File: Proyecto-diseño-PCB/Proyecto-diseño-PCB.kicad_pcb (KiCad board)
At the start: 4 copper layers, 76 x 35 mm, 41 parts, among them J1 USB_B_Micro, J2 PROGRAMACIÓN/DEPURACIÓN, J3 LADO A, J4 LADO B, SW1 BOTON, SW2 BOTON, SW3 RESET, U1 TPD2EUSB30, U2 LP2950-3.3_TO252, U3 PIC18LF45K50-I/P

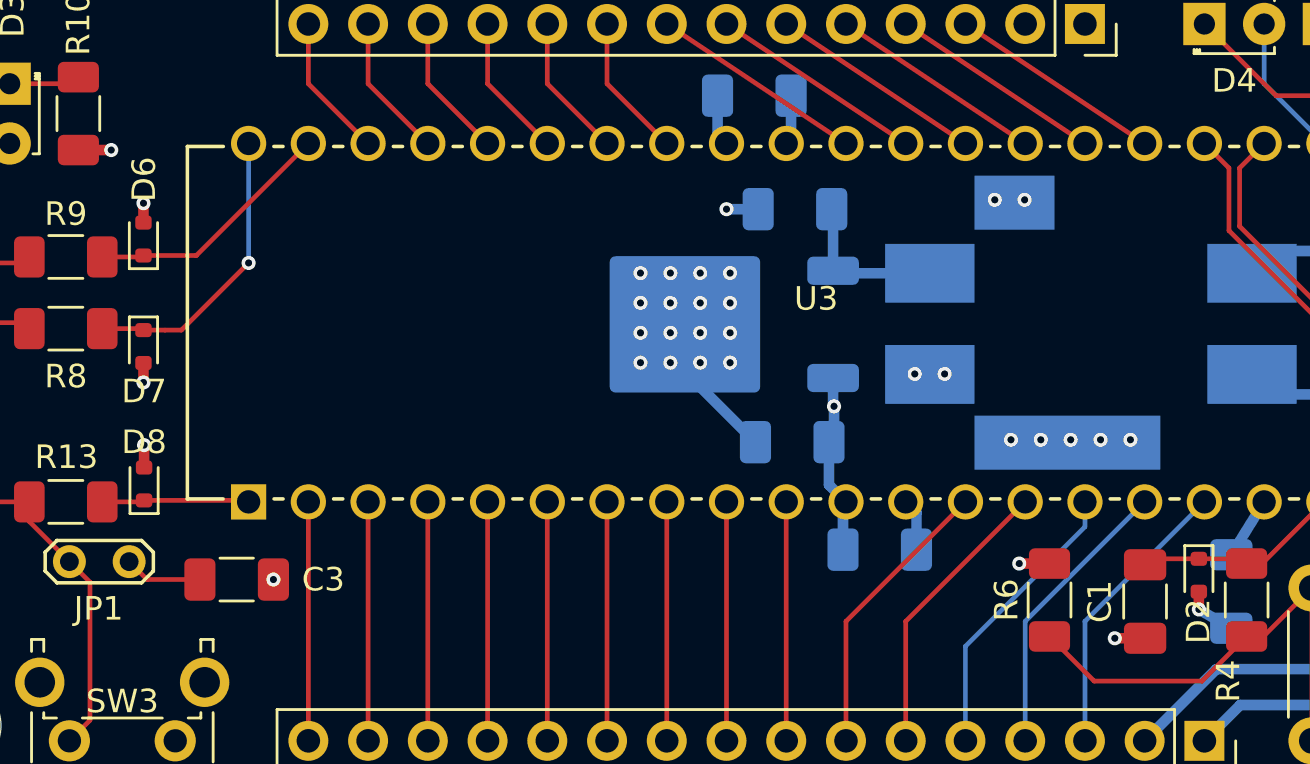
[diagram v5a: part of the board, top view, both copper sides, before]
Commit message: Correccion: agregue isla para disipacion de calor
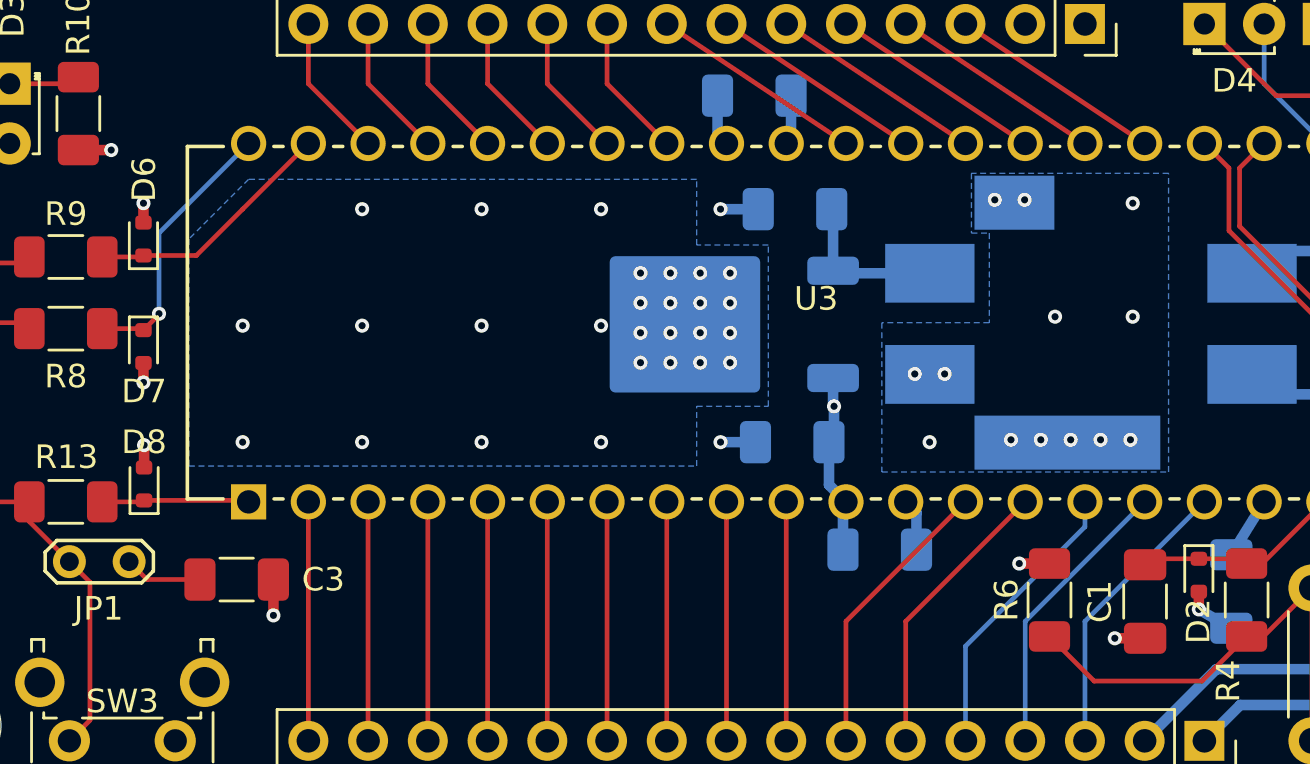
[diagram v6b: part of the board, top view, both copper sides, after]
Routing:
- net GND: track 41.0 -> 40.0 mm, vias 39 -> 55
- net /PGD: track 12.5 -> 11.6 mm
- added copper zone on B.Cu, net GND
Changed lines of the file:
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@@
 		(allow_soldermask_bridges_in_footprints no)
 		(tenting front back)
-		(grid_origin 164.719 98.298)
+		(grid_origin 124.079 88.138)
 		(pcbplotparams
 			(layerselection 0x00000000_00000000_55555555_55555555)
@@
 	)
 	(segment
+		(start 125.1335 92.964)
+		(end 125.1335 91.44)
+		(width 0.45)
+		(layer "F.Cu")
+		(net 1)
+	)
+	(segment
 		(start 176.911 87.692)
 		(end 176.911 86.868)
@@
 	)
 	(via
+		(at 128.905 85.598)
+		(size 0.6)
+		(drill 0.3)
+		(layers "F.Cu" "B.Cu")
+		(free yes)
+		(net 1)
+	)
+	(via
+		(at 161.671 75.438)
+		(size 0.6)
+		(drill 0.3)
+		(layers "F.Cu" "B.Cu")
+		(free yes)
+		(net 1)
+	)
+	(via
 		(at 144.5514 78.4098)
 		(size 0.6)
@@
 	)
 	(via
+		(at 158.369 80.264)
+		(size 0.6)
+		(drill 0.3)
+		(layers "F.Cu" "B.Cu")
+		(free yes)
+		(net 1)
+	)
+	(via
 		(at 155.804484 75.294914)
 		(size 0.6)
@@
 	)
 	(via
+		(at 144.145 75.692)
+		(size 0.6)
+		(drill 0.3)
+		(layers "F.Cu" "B.Cu")
+		(free yes)
+		(net 1)
+	)
+	(via
 		(at 142.0114 82.2198)
 		(size 0.6)
@@
 	)
 	(via
+		(at 144.145 85.598)
+		(size 0.6)
+		(drill 0.3)
+		(layers "F.Cu" "B.Cu")
+		(free yes)
+		(net 1)
+	)
+	(via
 		(at 140.7414 79.6798)
 		(size 0.6)
@@
 	)
 	(via
-		(at 144.399 75.692)
+		(at 133.985 75.692)
+		(size 0.6)
+		(drill 0.3)
+		(layers "F.Cu" "B.Cu")
+		(free yes)
+		(net 1)
+	)
+	(via
+		(at 123.825 80.645)
 		(size 0.6)
 		(drill 0.3)
 		(layers "F.Cu" "B.Cu")
+		(free yes)
 		(net 1)
 	)
@@
 	)
 	(via
+		(at 139.065 75.692)
+		(size 0.6)
+		(drill 0.3)
+		(layers "F.Cu" "B.Cu")
+		(free yes)
+		(net 1)
+	)
+	(via
+		(at 123.825 85.598)
+		(size 0.6)
+		(drill 0.3)
+		(layers "F.Cu" "B.Cu")
+		(free yes)
+		(net 1)
+	)
+	(via
 		(at 157.074484 75.294914)
 		(size 0.6)
@@
 	)
 	(via
+		(at 128.905 80.645)
+		(size 0.6)
+		(drill 0.3)
+		(layers "F.Cu" "B.Cu")
+		(free yes)
+		(net 1)
+	)
+	(via
 		(at 160.303654 85.497713)
 		(size 0.6)
@@
 	)
 	(via
-		(at 125.1335 91.44)
+		(at 133.985 85.598)
+		(size 0.6)
+		(drill 0.3)
+		(layers "F.Cu" "B.Cu")
+		(free yes)
+		(net 1)
+	)
+	(via
+		(at 125.1335 92.964)
 		(size 0.6)
 		(drill 0.3)
@@
 	)
 	(via
+		(at 161.671 80.264)
+		(size 0.6)
+		(drill 0.3)
+		(layers "F.Cu" "B.Cu")
+		(free yes)
+		(net 1)
+	)
+	(via
+		(at 139.065 80.645)
+		(size 0.6)
+		(drill 0.3)
+		(layers "F.Cu" "B.Cu")
+		(free yes)
+		(net 1)
+	)
+	(via
 		(at 142.0114 78.4098)
 		(size 0.6)
@@
 	)
 	(via
+		(at 153.035 85.598)
+		(size 0.6)
+		(drill 0.3)
+		(layers "F.Cu" "B.Cu")
+		(free yes)
+		(net 1)
+	)
+	(via
 		(at 119.608 83.058)
 		(size 0.6)
@@
 	)
 	(via
+		(at 139.065 85.598)
+		(size 0.6)
+		(drill 0.3)
+		(layers "F.Cu" "B.Cu")
+		(free yes)
+		(net 1)
+	)
+	(via
 		(at 142.0114 79.6798)
 		(size 0.6)
@@
 	)
 	(via
+		(at 133.985 80.645)
+		(size 0.6)
+		(drill 0.3)
+		(layers "F.Cu" "B.Cu")
+		(free yes)
+		(net 1)
+	)
+	(via
+		(at 128.905 75.692)
+		(size 0.6)
+		(drill 0.3)
+		(layers "F.Cu" "B.Cu")
+		(free yes)
+		(net 1)
+	)
+	(via
 		(at 118.237 73.178)
 		(size 0.6)
@@
 	)
 	(segment
-		(start 144.399 75.692)
-		(end 145.747 75.692)
-		(width 0.45)
-		(layer "B.Cu")
-		(net 1)
-	)
-	(segment
 		(start 164.483 92.71)
 		(end 165.862 93.5105)
@@
 	)
 	(segment
+		(start 144.145 75.692)
+		(end 145.747 75.692)
+		(width 0.45)
+		(layer "B.Cu")
+		(net 1)
+	)
+	(segment
 		(start 152.477 88.596)
 		(end 152.019 88.138)
@@
 	)
 	(segment
-		(start 180.594 84.455)
-		(end 182.671 84.455)
+		(start 144.145 85.598)
+		(end 145.6305 85.598)
 		(width 0.45)
 		(layer "B.Cu")
@@
 	)
 	(segment
-		(start 171.691 80.217)
-		(end 172.593 80.217)
+		(start 180.594 84.455)
+		(end 182.671 84.455)
 		(width 0.45)
 		(layer "B.Cu")
@@
 	)
 	(segment
-		(start 145.6305 85.598)
-		(end 142.631 82.5985)
+		(start 171.691 80.217)
+		(end 172.593 80.217)
 		(width 0.45)
 		(layer "B.Cu")
@@
 	)
 	(segment
+		(start 123.825 75.692)
+		(end 126.619 72.898)
+		(width 0.2)
+		(layer "F.Cu")
+		(net 11)
+	)
+	(segment
 		(start 117.856 77.724)
 		(end 119.546 77.724)
@@
 	(segment
 		(start 121.855 77.662)
-		(end 126.619 72.898)
+		(end 123.825 75.692)
 		(width 0.2)
 		(layer "F.Cu")
@@
 	)
 	(segment
-		(start 117.856 80.772)
-		(end 119.546 80.772)
-		(width 0.2)
-		(layer "F.Cu")
-		(net 12)
-	)
-	(segment
-		(start 121.223 80.834)
-		(end 124.079 77.978)
+		(start 120.269 80.173)
+		(end 119.608 80.834)
 		(width 0.2)
 		(layer "F.Cu")
@@
 	)
 	(segment
-		(start 120.523 80.834)
-		(end 121.223 80.834)
+		(start 117.856 80.772)
+		(end 119.546 80.772)
 		(width 0.2)
 		(layer "F.Cu")
@@
 	)
 	(segment
-		(start 119.608 80.834)
-		(end 120.523 80.834)
+		(start 120.269 80.137)
+		(end 120.269 80.173)
 		(width 0.2)
 		(layer "F.Cu")
@@
 	)
 	(via
-		(at 124.079 77.978)
+		(at 120.269 80.137)
 		(size 0.6)
 		(drill 0.3)
@@
 	)
 	(segment
-		(start 124.079 77.978)
+		(start 120.269 76.708)
 		(end 124.079 72.898)
 		(width 0.2)
@@
 	)
 	(segment
+		(start 120.269 80.137)
+		(end 120.269 76.708)
+		(width 0.2)
+		(layer "B.Cu")
+		(net 12)
+	)
+	(segment
 		(start 119.572 88.138)
 		(end 119.634 88.076)
@@
 	)
 	(zone
+		(net 1)
+		(net_name "GND")
+		(layer "B.Cu")
+		(hatch edge 0.5)
+		(priority 3)
+		(connect_pads no
+			(clearance 0.5)
+		)
+		(min_thickness 0.25)
+		(filled_areas_thickness no)
+		(fill yes
+			(thermal_gap 0.5)
+			(thermal_bridge_width 0.5)
+			(smoothing fillet)
+			(radius 0.508)
+		)
+		(polygon
+			(pts
+				(xy 151.003 86.868) (xy 163.195 86.868) (xy 163.195 74.168) (xy 154.813 74.168) (xy 154.813 76.708)
+				(xy 155.575 76.708) (xy 155.575 80.518) (xy 151.003 80.518)
+			)
+		)
+	)
+	(zone
+		(net 1)
+		(net_name "GND")
+		(layer "B.Cu")
+		(hatch edge 0.5)
+		(priority 2)
+		(connect_pads yes
+			(clearance 0.5)
+		)
+		(min_thickness 0.25)
+		(filled_areas_thickness no)
+		(fill yes
+			(thermal_gap 0.5)
+			(thermal_bridge_width 0.5)
+			(smoothing fillet)
+			(radius 1.27)
+		)
+		(polygon
+			(pts
+				(xy 143.129 77.216) (xy 143.129 74.422) (xy 124.079 74.422) (xy 121.539 76.962) (xy 121.539 86.614)
+				(xy 143.129 86.614) (xy 143.129 84.074) (xy 146.177 84.074) (xy 146.177 77.216)
+			)
+		)
+	)
+	(zone
